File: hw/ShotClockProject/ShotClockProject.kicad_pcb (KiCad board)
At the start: 2 copper layers, 117 parts, among them IC1 TP4056-42-ESOP8_Rearanged, J1 USB4120-03-C_REVA, J10 DW254W-22-20-85, J2 Conn_ST_STDC14, J3 Conn_01x06_Pin, J4 SM03B-SRSS-TB(LF)(SN)(P), J5 Conn_01x02_Pin, J6 Conn_01x03_Pin, J7 DW254W-22-20-85, J8 DW254W-22-20-85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

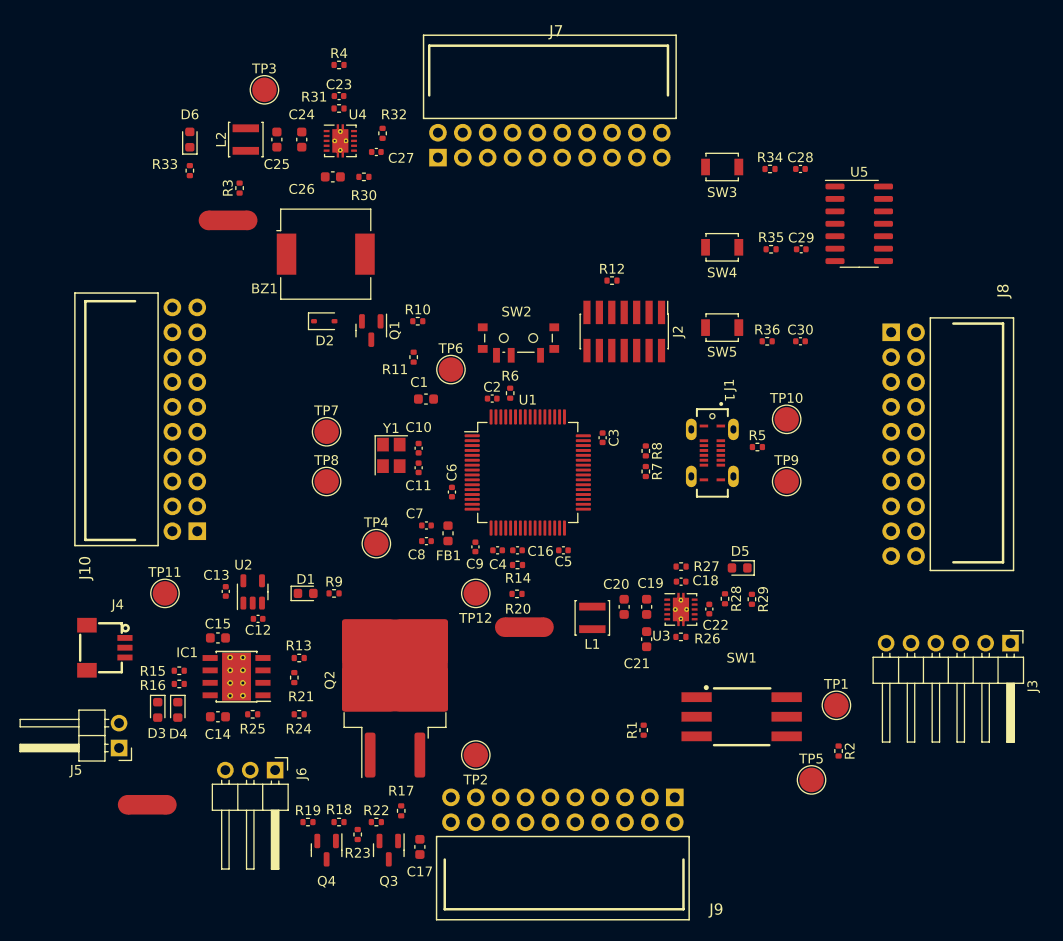
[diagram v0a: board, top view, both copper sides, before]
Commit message: Added outline to main print
71.8x71.8mm
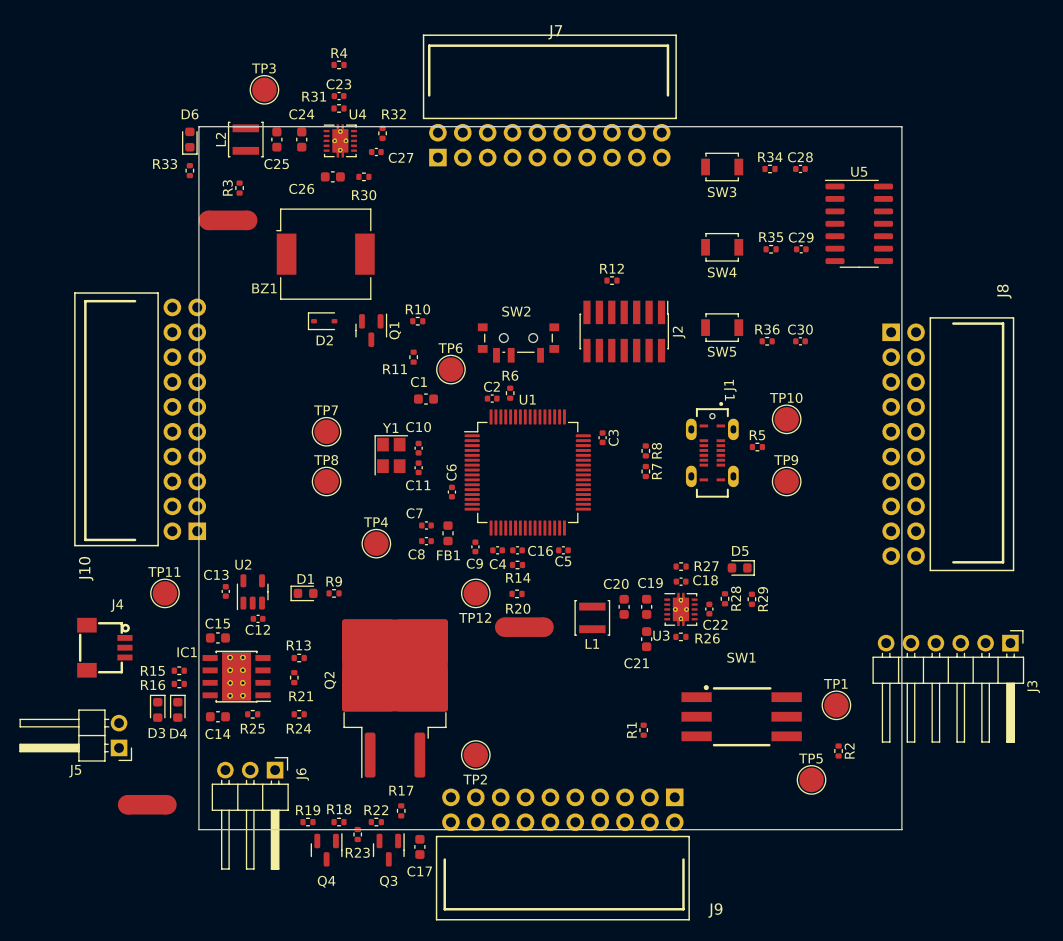
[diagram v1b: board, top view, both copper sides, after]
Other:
- board outline added: 71.8 x 71.8 mm
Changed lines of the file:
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@@
     )
   )
+  (gr_rect (start 113.96 60.28) (end 185.76 132.08)
+    (stroke (width 0.1) (type default)) (fill none) (layer "Edge.Cuts"))
 )

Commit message: Add FPC conenctors
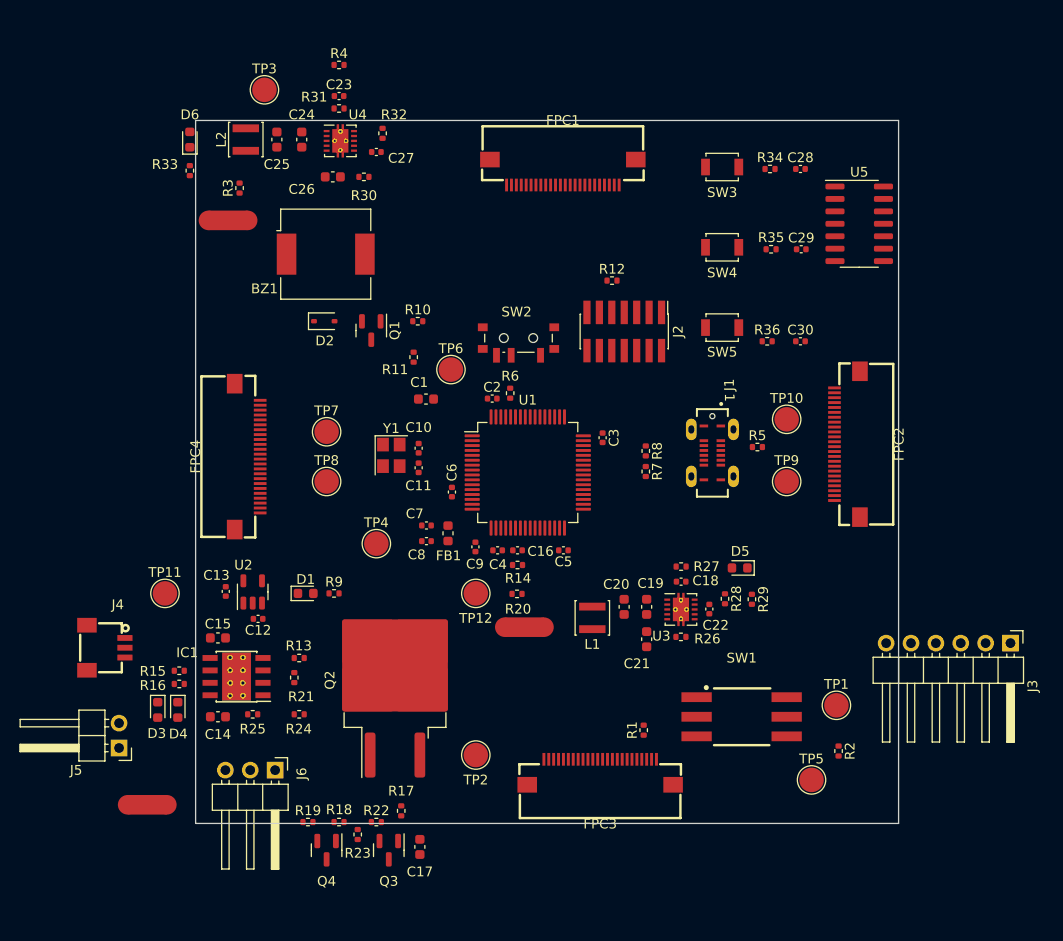
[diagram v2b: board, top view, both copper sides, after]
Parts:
- removed J10, J7, J8, J9: DW254W-22-20-85, DW254W-22-20-85:CONN-TH_20P-P2.54_DEALON_DW254W-22-20-85
- added FPC1: AFC01-S24FCA-00, AFC01-S24FCA-00:FPC-SMD_P0.50-24P_FGS-XJ-H2.0, F.Cu at (151.1, 64.9)
- added FPC2: AFC01-S24FCA-00, AFC01-S24FCA-00:FPC-SMD_P0.50-24P_FGS-XJ-H2.0, F.Cu at (180.2, 92.7)
- added FPC3: AFC01-S24FCA-00, AFC01-S24FCA-00:FPC-SMD_P0.50-24P_FGS-XJ-H2.0, F.Cu at (154.9, 126.2)
- added FPC4: AFC01-S24FCA-00, AFC01-S24FCA-00:FPC-SMD_P0.50-24P_FGS-XJ-H2.0, F.Cu at (118.9, 94.0)

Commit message: Redid layout with new board dimensions
Changed tactile switches to larger push switches (also momentary)
Changed USART1 to UART4 & added UART5 to STDC14 connector
Placed all components nearer to each other, and within the PCB outer edge
Added rounded corners
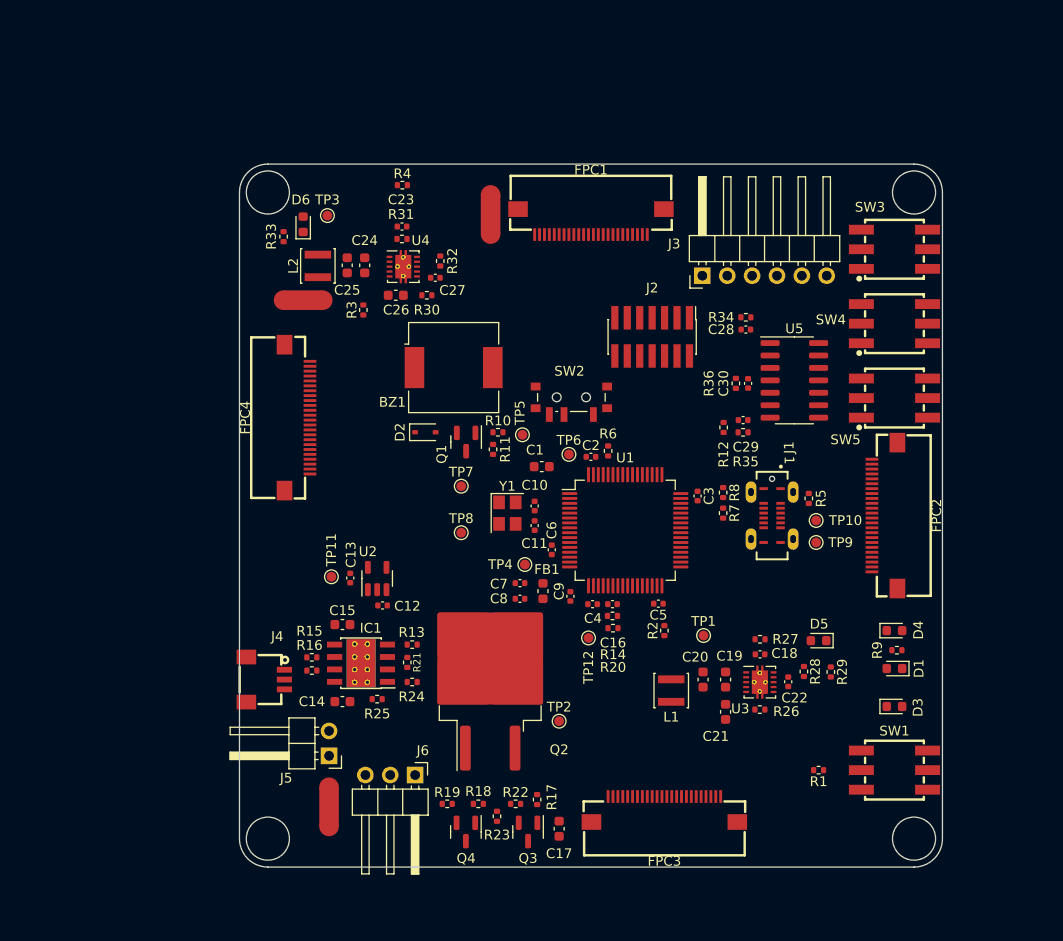
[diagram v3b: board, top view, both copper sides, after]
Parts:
- SW1: value PS-5824SVB-6PL -> TK-6580S-1; footprint PS-5824SVB-6PL:SW-SMD_6P-L5.8-W5.8-P2.00-LS11.3 -> TK-6580S-1:SW-SMD_TK-6580S-1
- SW3, SW4, SW5: value SW_SPST -> TK-6580S-2; footprint Button_Switch_SMD:SW_SPST_B3U-1000P -> TK-6580S-2:SW-SMD_TK-6580S-2
- TP1, TP10, TP11, TP12, TP2, TP3, TP4, TP5, TP6, TP7, TP8, TP9: footprint TestPoint:TestPoint_Pad_D2.5mm -> TestPoint:TestPoint_Pad_D1.0mm
- moved D3 75.3 mm to (185.0, 119.5), turned to 0 degrees
- moved D4 73.6 mm to (185.0, 111.8), turned to 0 degrees
- moved D1 60.6 mm to (185.0, 115.6), turned to 180 degrees
- moved R9 57.8 mm to (185.2, 113.8)
- moved J3 49.0 mm to (165.4, 75.5), turned to 90 degrees
- moved TP5 46.0 mm to (147.0, 91.8)
- moved NT2 42.3 mm to (143.8, 69.2), turned to -90 degrees
- moved R2 21.6 mm to (161.5, 111.8), turned to 90 degrees
- moved J5 21.5 mm to (127.2, 124.5)
- moved SW3 19.5 mm to (185.0, 72.8)
- moved SW4 19.3 mm to (185.0, 80.4)
- moved SW5 19.0 mm to (185.0, 88.0)
- moved R35 18.9 mm to (169.5, 91.5), turned to 180 degrees
- moved R12 18.8 mm to (167.6, 91.0), turned to -90 degrees
- moved NT1 18.6 mm to (127.2, 129.8), turned to 90 degrees
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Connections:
- D1 pad 1: GND -> Net-(D1-K)
- D1 pad 2: Net-(D1-A) -> /STM32F103RCT6/ORANGE_LED
- J2 pad 13: unconnected-(J2-VCP_RX-Pad13) -> /STM32F103RCT6/UART5_RX
- J2 pad 14: unconnected-(J2-VCP_TX-Pad14) -> /STM32F103RCT6/UART5_TX
- J3 pad 4: /STM32F103RCT6/USART1_RX -> /STM32F103RCT6/UART4_RX
- J3 pad 5: /STM32F103RCT6/USART1_TX -> /STM32F103RCT6/UART4_TX
- R9 pad 1: Net-(D1-A) -> GND
- R9 pad 2: /STM32F103RCT6/ORANGE_LED -> Net-(D1-K)
- SW1 pad 2: /Li-Po Battery and charger/charger_out -> unconnected-(SW1-Pad2)
- SW1 pad 3: Net-(R1-Pad1) -> unconnected-(SW1-Pad3)
- SW1 pad 5: unconnected-(SW1-Pad5) -> Net-(R1-Pad1)
- SW1 pad 6: unconnected-(SW1-Pad6) -> /Li-Po Battery and charger/charger_out
- U1 pad 35: /STM32F103RCT6/USART1_TX -> unconnected-(U1-PB14-Pad35)
- U1 pad 36: /STM32F103RCT6/USART1_RX -> unconnected-(U1-PB15-Pad36)
- U1 pad 51: unconnected-(U1-PC10-Pad51) -> /STM32F103RCT6/UART4_TX
- U1 pad 52: unconnected-(U1-PC11-Pad52) -> /STM32F103RCT6/UART4_RX
- U1 pad 53: unconnected-(U1-PC12-Pad53) -> /STM32F103RCT6/UART5_TX
- U1 pad 54: unconnected-(U1-PD2-Pad54) -> /STM32F103RCT6/UART5_RX
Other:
- outline, holes or cut-outs redrawn

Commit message: Moved components further from edge
Also changed hole size, hole placement further from edge and other small dimensional changes
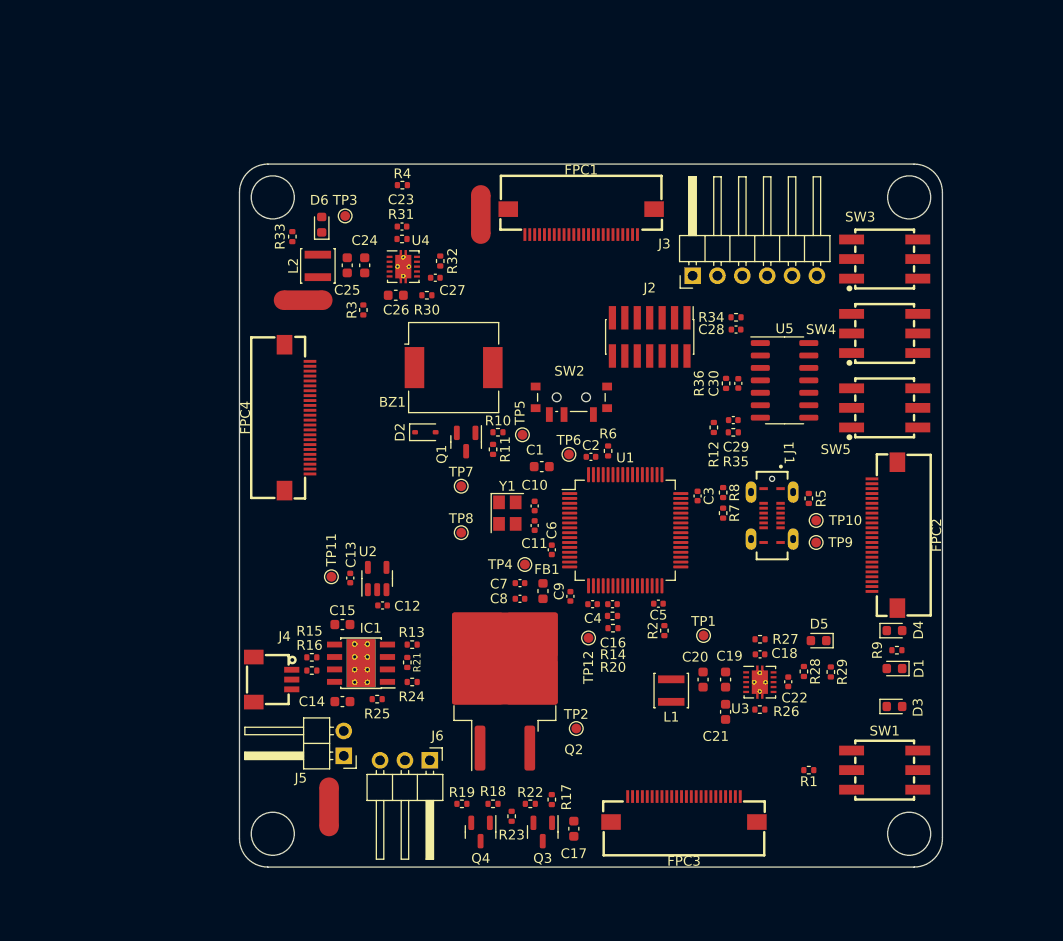
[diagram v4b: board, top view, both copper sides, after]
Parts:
- moved J6 2.12 mm to (137.5, 125.0)
- moved FPC2 2.00 mm to (184.0, 102.0)
- moved FPC3 2.00 mm to (163.5, 130.0)
- moved TP2 1.90 mm to (152.5, 121.8)
- moved D6 1.90 mm to (126.5, 70.3)
- moved TP3 1.82 mm to (128.9, 69.4)
- moved C17 1.50 mm to (152.2, 132.0)
- moved J5 1.50 mm to (128.8, 124.5)
- moved Q2 1.50 mm to (145.2, 116.1)
- moved Q3 1.50 mm to (149.1, 132.3)
- moved Q4 1.50 mm to (142.7, 132.3)
- moved R17 1.50 mm to (150.0, 129.0)
- moved R18 1.50 mm to (144.0, 129.4)
- moved R19 1.50 mm to (140.8, 129.4)
- moved R22 1.50 mm to (147.8, 129.4)
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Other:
- outline, holes or cut-outs redrawn

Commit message: Started on routing
Started with decoup caps, sensitive signals and simple GPIO
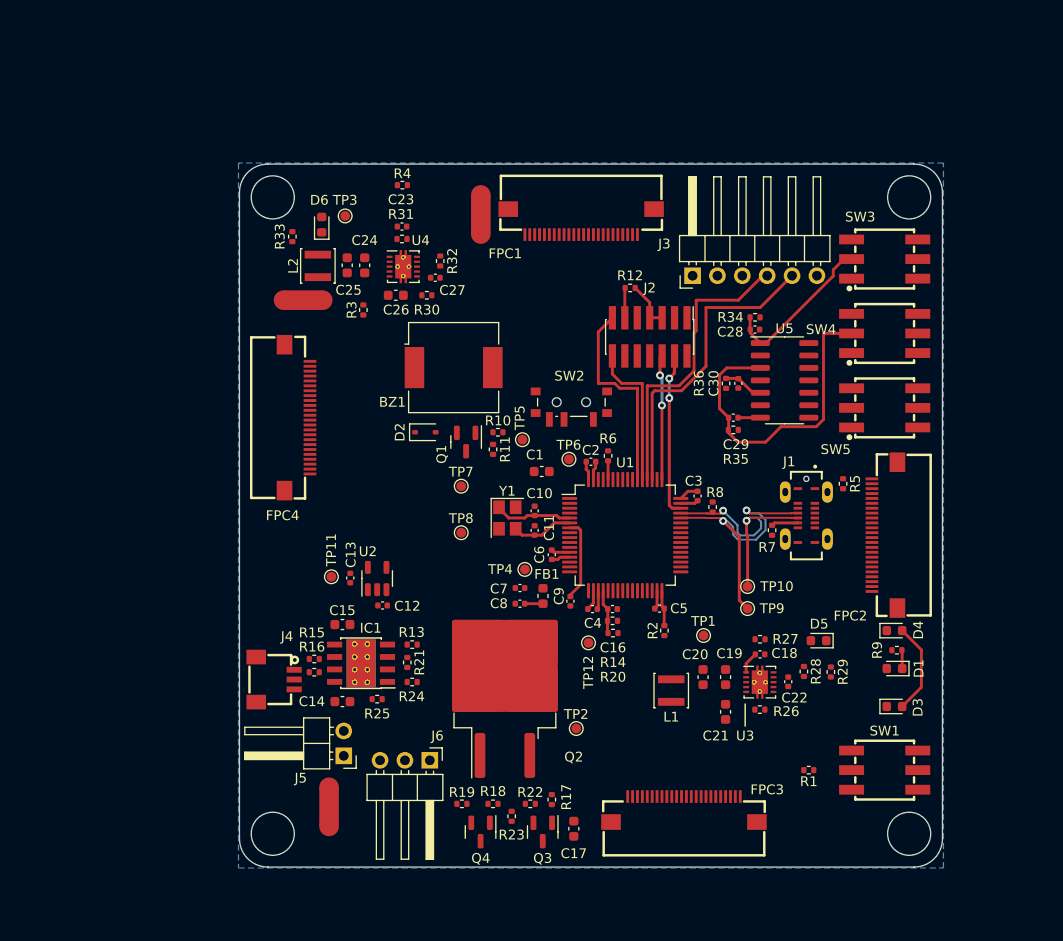
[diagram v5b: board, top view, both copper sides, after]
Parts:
- moved R12 16.6 mm to (158.0, 76.8), turned to 0 degrees
- moved TP10 9.72 mm to (170.0, 107.2)
- moved TP9 9.72 mm to (170.0, 109.5)
- moved R7 5.30 mm to (172.5, 101.5)
- moved R5 3.81 mm to (179.8, 96.8)
- moved J1 3.50 mm to (176.0, 100.0)
- moved R34 1.94 mm to (170.8, 79.8)
- moved C28 1.93 mm to (170.8, 81.0)
- moved R8 1.83 mm to (166.4, 99.1)
- moved Q2 0.75 mm to (145.2, 116.8)
- moved C5 0.51 mm to (161.0, 109.5)
- moved C1 0.50 mm to (149.0, 95.5)
- moved C10 0.50 mm to (148.2, 99.5)
- moved C11 0.50 mm to (148.2, 101.5)
- moved C16 0.50 mm to (156.2, 109.5)
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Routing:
- net Net-(U5-2A): track 0.00 -> 33.4 mm
- net /STM32F103RCT6/UART4_TX: track 0.00 -> 31.6 mm
- net /STM32F103RCT6/UART4_RX: track 0.00 -> 30.6 mm
- net /STM32F103RCT6/USB_D-: track 0.00 -> 29.2 mm, vias 0 -> 2
- net /STM32F103RCT6/USB_D+: track 0.00 -> 24.8 mm, vias 0 -> 2
- net /STM32F103RCT6/UART5_RX: track 0.00 -> 20.8 mm
- net GND: track 0.00 -> 16.9 mm
- net /STM32F103RCT6/SWDIO: track 0.00 -> 16.8 mm, vias 0 -> 2
- net Net-(U5-1A): track 0.00 -> 16.3 mm
- net /STM32F103RCT6/UART5_TX: track 0.00 -> 16.0 mm
- net /STM32F103RCT6/SWCLK: track 0.00 -> 12.8 mm, vias 0 -> 2
- net +3.3V: track 0.00 -> 11.4 mm
- net Net-(D3-A): track 0.00 -> 9.38 mm
- net /STM32F103RCT6/NRST: track 0.00 -> 8.43 mm
- net /STM32F103RCT6/HSE_IN: track 0.00 -> 7.94 mm
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- added copper zone on B.Cu, net GND

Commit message: Routed almost everything, except display connector
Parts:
- moved NT3 11.1 mm to (128.7, 67.7)
- moved C9 8.66 mm to (144.7, 104.0), turned to 180 degrees
- moved TP10 5.53 mm to (164.8, 109.1)
- moved C25 5.01 mm to (132.5, 70.8), turned to 90 degrees
- moved TP12 4.81 mm to (158.5, 112.2)
- moved C19 4.74 mm to (163.2, 118.0), turned to 0 degrees
- moved L2 4.65 mm to (130.8, 74.8)
- moved NT2 4.65 mm to (138.4, 67.6)
- moved L1 4.63 mm to (166.8, 117.0)
- moved C20 3.97 mm to (163.2, 119.8), turned to 0 degrees
- moved NT1 3.95 mm to (130.5, 127.5), turned to 180 degrees
- moved TP2 3.89 mm to (155.2, 124.5)
- moved C24 3.69 mm to (130.7, 70.8), turned to 90 degrees
- moved R3 3.36 mm to (133.2, 81.2)
- moved TP9 2.84 mm to (167.2, 109.0)
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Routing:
- net +5V: track 0.00 -> 249.6 mm, vias 0 -> 2
- net GND: track 16.9 -> 138.0 mm, vias 0 -> 58
- net +BATT: track 0.00 -> 108.5 mm
- net Net-(D4-K): track 0.00 -> 104.2 mm, vias 0 -> 2
- net Net-(D3-A): track 9.38 -> 110.9 mm, vias 0 -> 3
- net Net-(D3-K): track 0.00 -> 93.9 mm, vias 0 -> 2
- net /Connectors to segment displays/DISP1_SEG_G: track 0.00 -> 62.9 mm, vias 0 -> 2
- net /Connectors to segment displays/DISP2_SEG_E: track 0.00 -> 60.1 mm, vias 0 -> 2
- net /Connectors to segment displays/DISP1_SEG_F: track 0.00 -> 57.5 mm, vias 0 -> 2
- net /Connectors to segment displays/TIM2_CH2_PWM2_SEG: track 0.00 -> 56.4 mm, vias 0 -> 2
- net /Connectors to segment displays/DISP2_SEG_D: track 0.00 -> 51.0 mm, vias 0 -> 2
- net /Connectors to segment displays/DISP1_SEG_D: track 0.00 -> 48.2 mm, vias 0 -> 2
- net /Connectors to segment displays/TIM2_CH1_PWM1_SEG: track 0.00 -> 43.0 mm, vias 0 -> 2
- net /Connectors to segment displays/DISP1_SEG_A: track 0.00 -> 43.0 mm, vias 0 -> 3
- net /Connectors to segment displays/DISP1_SEG_C: track 0.00 -> 40.1 mm, vias 0 -> 2
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- added copper zone on In2.Cu, net +3.3V
- added copper zone on In1.Cu, net GND
- removed copper zone on B.Cu, net GND
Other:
- copper layers 2 -> 4
